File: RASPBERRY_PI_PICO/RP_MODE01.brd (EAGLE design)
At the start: 100 x 100 mm, 38 parts, among them U2 RA-02_LORA

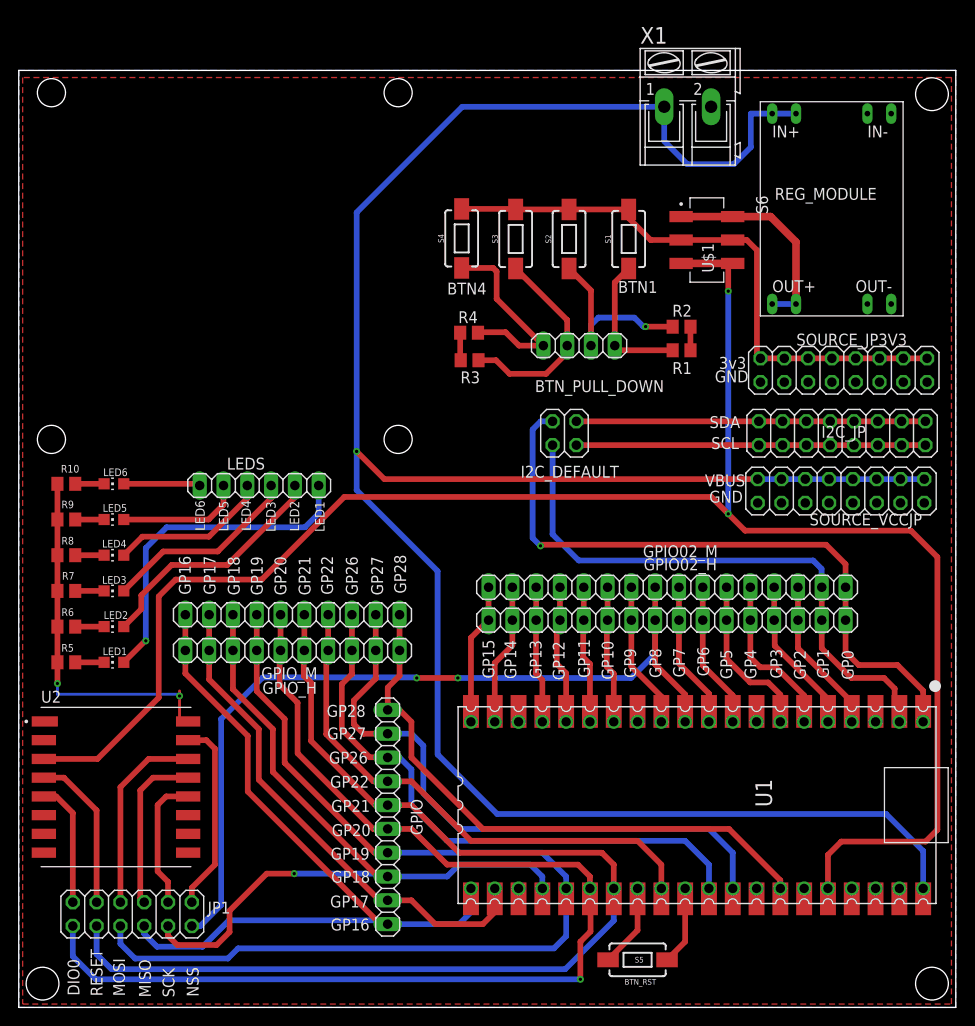
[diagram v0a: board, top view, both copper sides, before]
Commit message: Se actualiza PCB
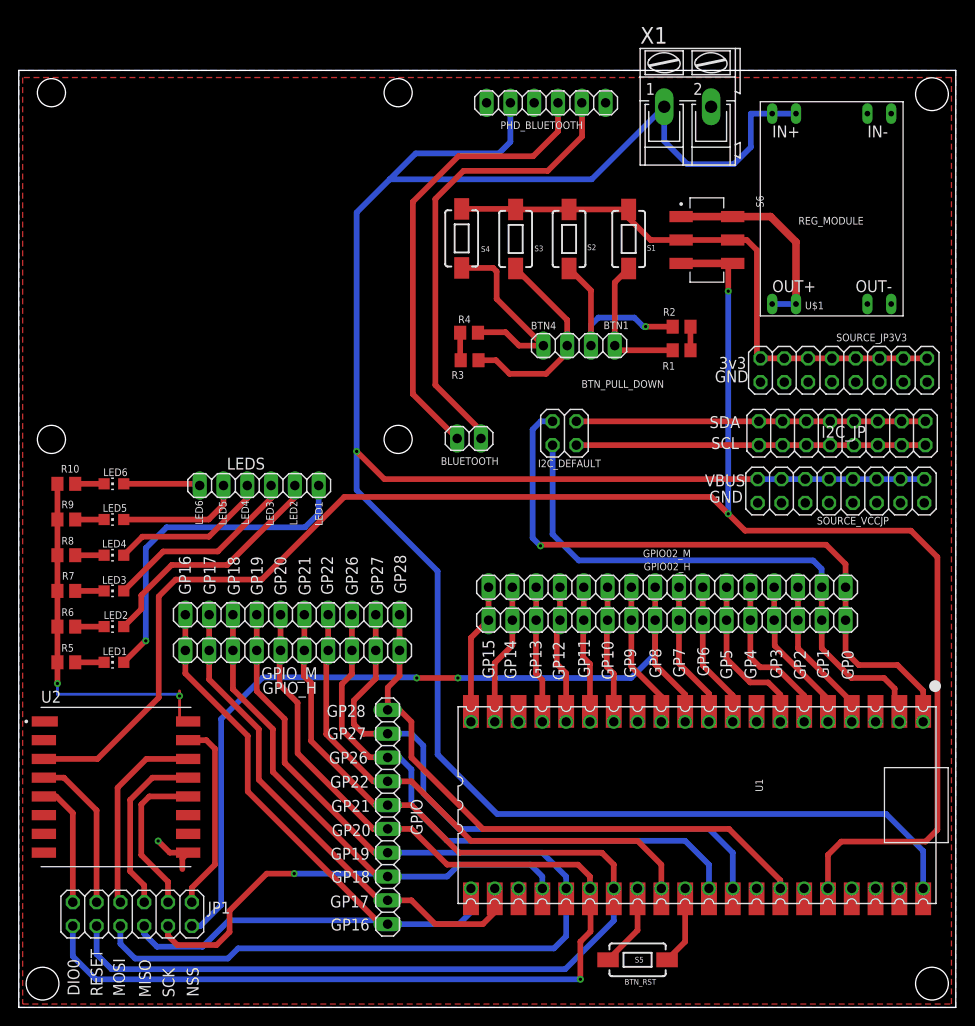
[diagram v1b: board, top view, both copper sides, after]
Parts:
- added BLUETOOTH: (no value), pinhead:1X02
- added PHD_BLUETOOTH: (no value), pinhead:1X06
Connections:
- new net ENABLE: PHD_BLUETOOTH.1
- new net RX: BLUETOOTH.1, PHD_BLUETOOTH.5
- new net TX: BLUETOOTH.2, PHD_BLUETOOTH.4
- net GND: now also PHD_BLUETOOTH.3
- net VBUS: now also PHD_BLUETOOTH.2
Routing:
- net RX: track 0.00 -> 49.6 mm
- net TX: track 0.00 -> 48.9 mm
- net VBUS: track 243.9 -> 263.7 mm
- net GND: track 54.2 -> 68.8 mm, vias 2 -> 3
- net SCK: track 14.5 -> 17.0 mm
- net VSYS: track 0.00 -> 1.11 mm
- net GP9: track 14.6 -> 15.7 mm
- net GP8: track 91.3 -> 92.4 mm
- net GP7: track 14.6 -> 15.7 mm
- net GP6: track 14.6 -> 15.7 mm
- net GP5: track 16.8 -> 17.9 mm
- net GP4: track 16.6 -> 17.7 mm
- net GP3: track 15.6 -> 16.7 mm
- net GP27: track 65.6 -> 66.7 mm
- net GP26: track 62.6 -> 63.7 mm
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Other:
- board text added: "RX_BT"
- board text added: "TX_BT"
